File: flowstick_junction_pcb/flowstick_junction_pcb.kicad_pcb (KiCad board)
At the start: 4 copper layers, 13.5 x 12.4 mm, 8 parts, among them J1 Conn_01x01_Pin, J2 Conn_01x01_Pin, J3 Conn_01x01_Pin, J4 Conn_01x01_Pin, J5 LED1, J6 LED2, J7 LED3, J8 LED4

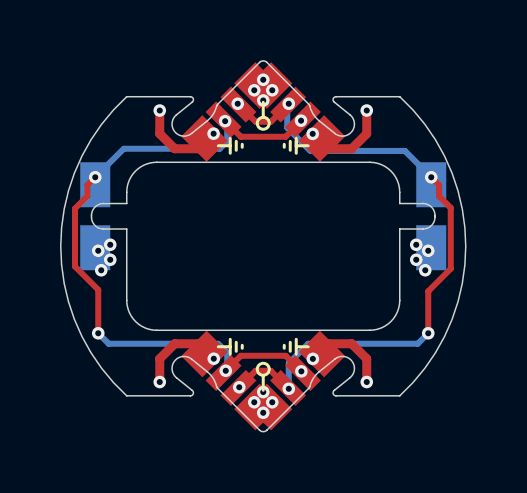
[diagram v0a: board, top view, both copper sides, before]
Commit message: work on rev2 + panelize LED strips
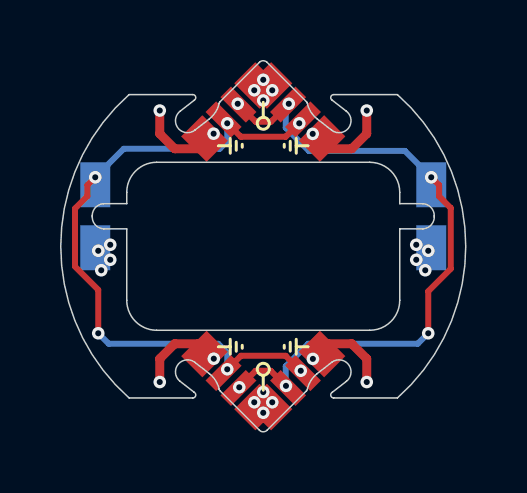
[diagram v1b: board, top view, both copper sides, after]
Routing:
- net /LED_DAT: track 22.8 -> 22.2 mm
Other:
- outline, holes or cut-outs redrawn

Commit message: Final rev2, probably
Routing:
- net /LED_CLK: track 22.5 -> 23.7 mm
- net /LED_DAT: track 22.2 -> 23.4 mm
